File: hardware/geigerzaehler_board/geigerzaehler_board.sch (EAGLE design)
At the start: 24 parts, among them IC1 IRFDC20, IC2 MC34063AP, IC3 40106N, Q1 BC327, X1 GMSTBV2

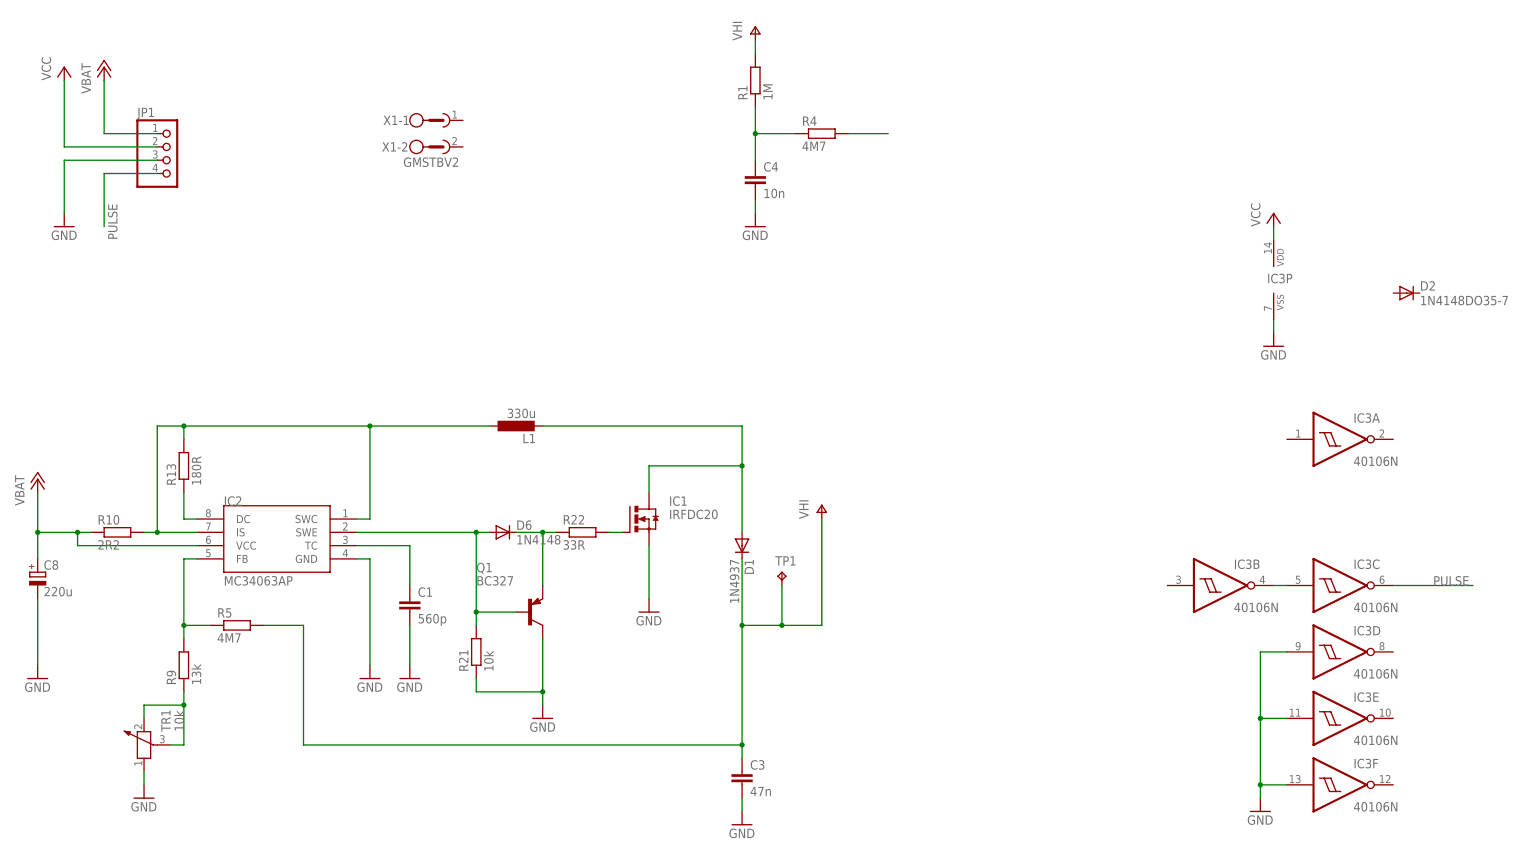
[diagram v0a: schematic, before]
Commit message: completed first version of geigerzähler-board
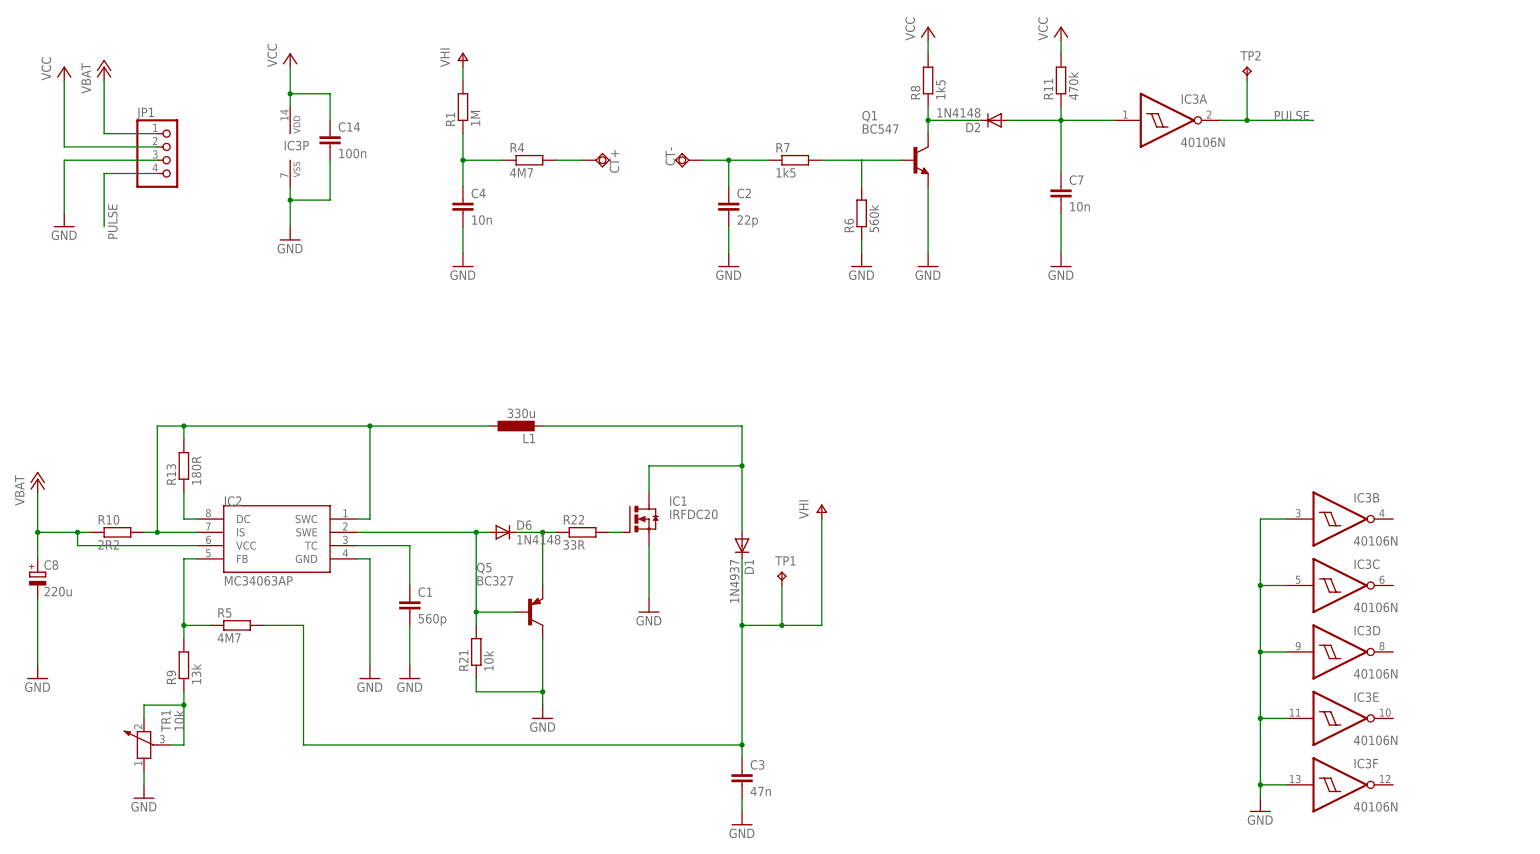
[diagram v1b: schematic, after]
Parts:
- removed X1: GMSTBV2, con-phoenix-762:GMSTBV2
- added C14: 100n, rcl:C-EU050-025X075
- added C2: 22p, rcl:C-EU025-025X050
- added C7: 10n, rcl:C-EU050-025X075
- added CT+, CT-: TPSQPAD1-13Y, testpad:TPSQPAD1-13Y
- added Q5: BC327, transistor-pnp:BC327
- added R11: 470k, rcl:R-EU_0207/10
- added R6: 560k, rcl:R-EU_0207/10
- added R7, R8: 1k5, rcl:R-EU_0207/10
- added TP2: TPPAD1-13Y, testpad:TPPAD1-13Y
- D2: value 1N4148DO35-7 -> 1N4148; device diode:1N4148DO35-7 -> diode:1N4148DO35-10
- Q1: value BC327 -> BC547; device transistor-pnp:BC327 -> transistor:BC547
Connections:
- removed net N$10: IC3B.O, IC3C.I
- new net N$13: C2.1, CT-.TP, R7.1
- new net N$14: Q1.B, R6.2, R7.2
- new net N$15: D2.C, Q1.C, R8.1
- new net N$16: C7.1, D2.A, IC3A.I, R11.1
- net GND: now also C14.2, C2.2, C7.2, IC3B.I, IC3C.I, Q1.E, Q5.C, R6.1; no longer Q1.C
- net N$1: now also Q5.B; no longer Q1.B
- net N$12: now also CT+.TP
- net N$2: now also Q5.E; no longer Q1.E
- net PULSE: now also IC3A.O, TP2.TP; no longer IC3C.O
- net VCC: now also C14.1, R11.2, R8.2
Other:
- moved on the sheet: C4, D2, IC3A, IC3B, IC3P, R1, R4

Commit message: optimized geigerzähler-board
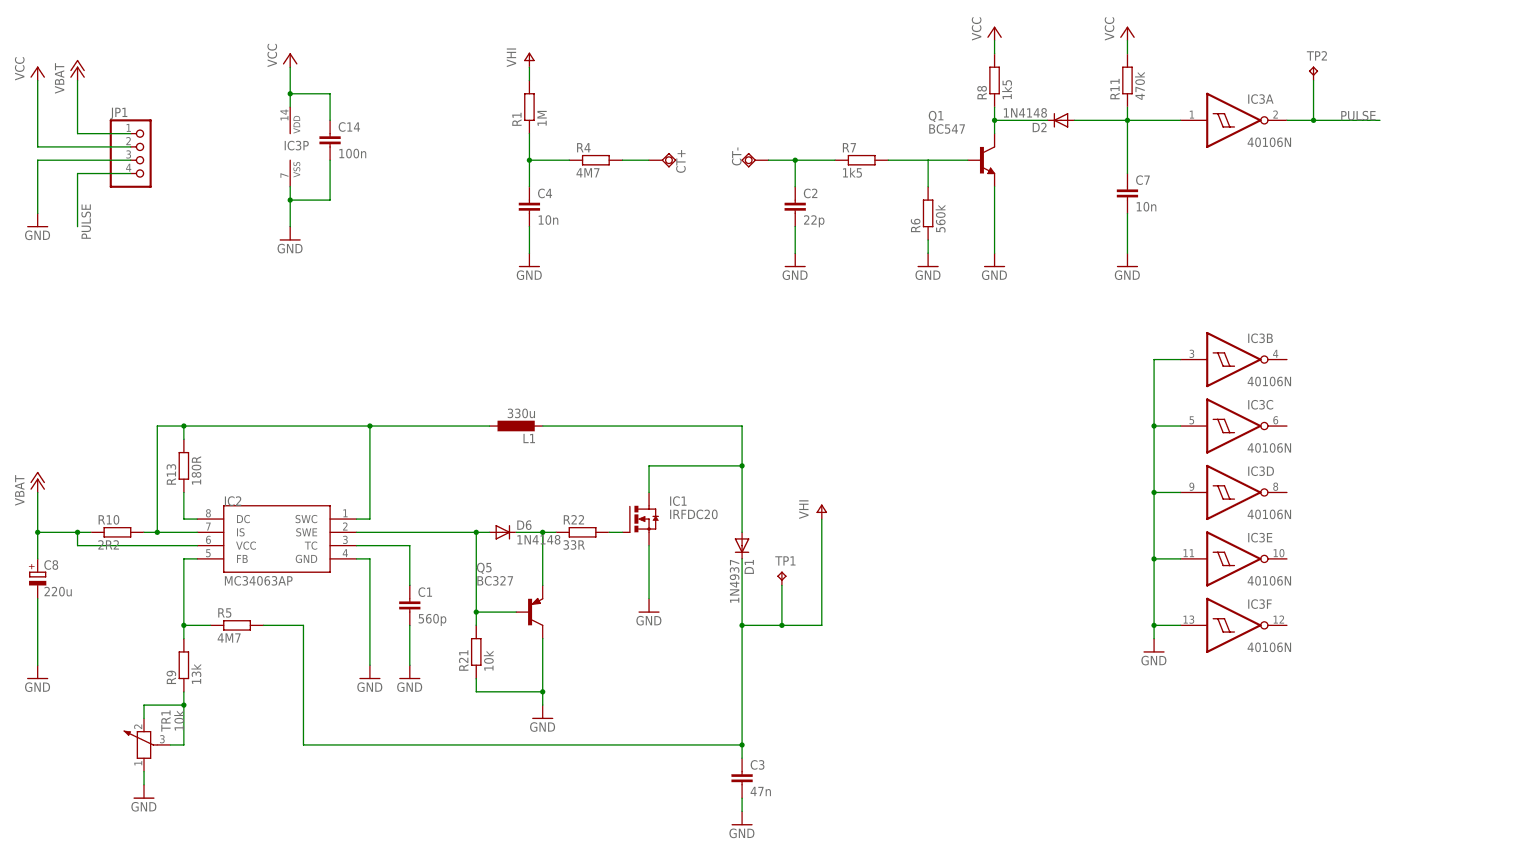
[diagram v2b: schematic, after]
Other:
- moved on the sheet: C2, C4, C7, CT+, CT-, D2, IC3A, IC3B, IC3C, IC3D, IC3E, IC3F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
